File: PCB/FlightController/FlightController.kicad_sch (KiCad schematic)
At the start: 13 parts, among them J1 SMA Connector, J2 BATT IN, J3 BATT OUT, J4 BATT Reg IC, J5 Pump, J6 HallCircuit, U1 XIAO-nRF52840-DIP, U2 RFM95W

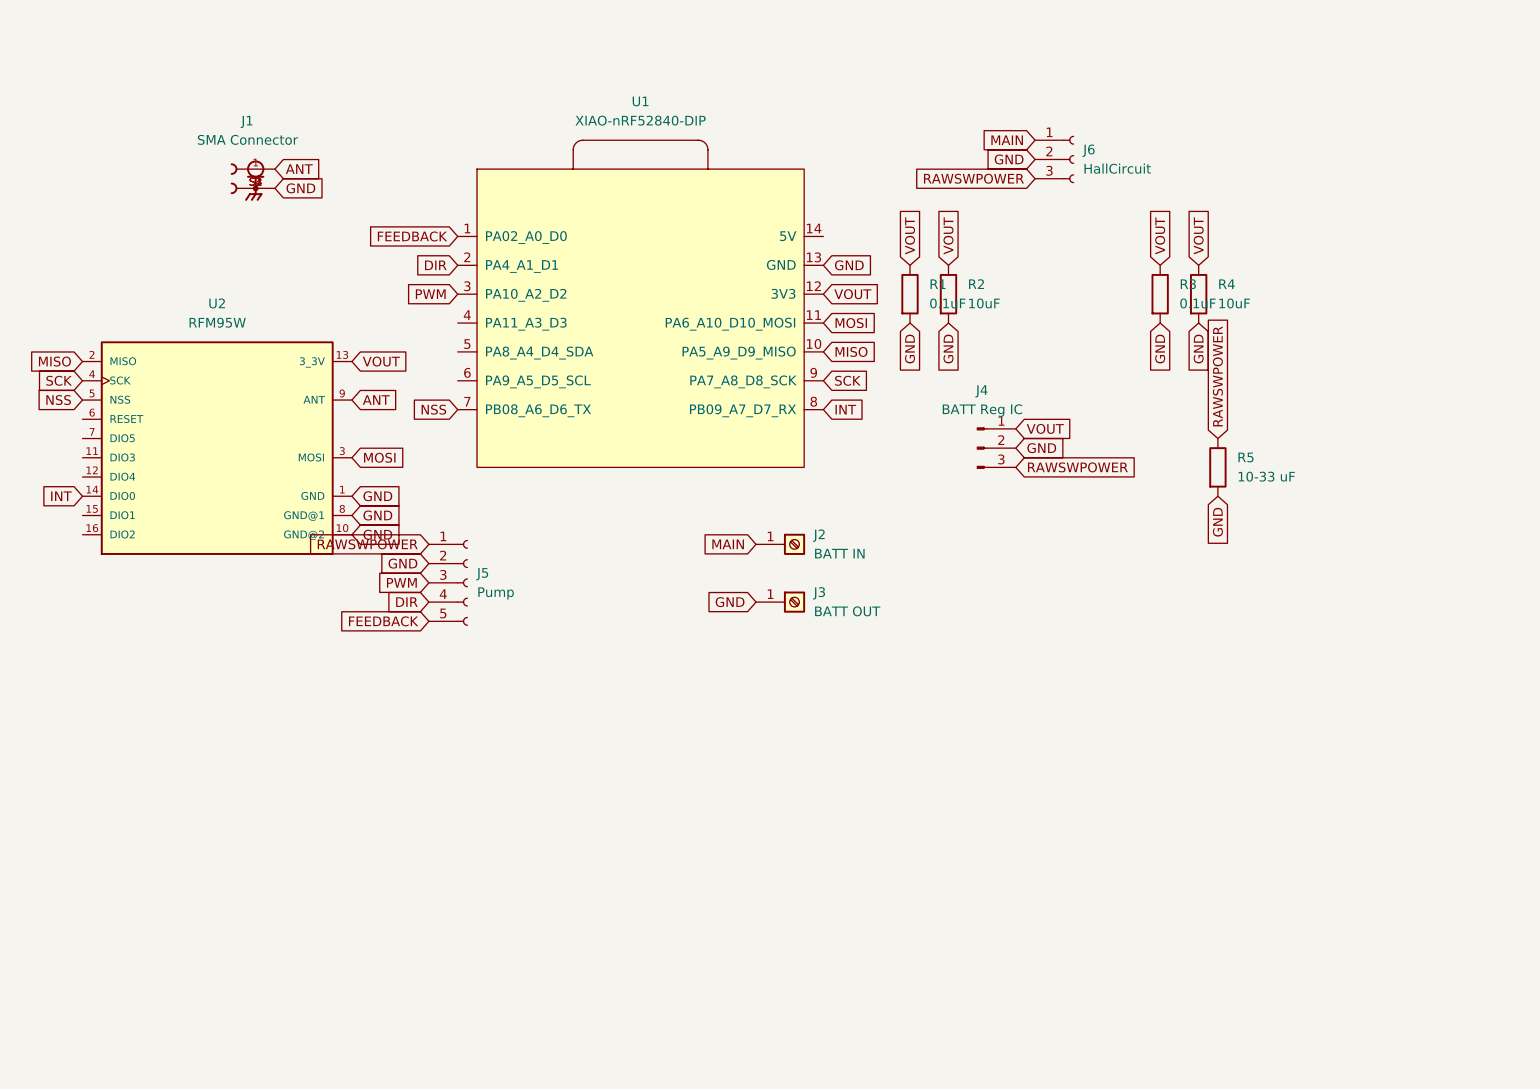
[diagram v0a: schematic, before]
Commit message: added a P-mosfet for the 3.3v wiring and let the 3.3v regulator "pre-power" the (now 4) pin switch system for the hall effect magnet sensor.
added a P-mosfet for the 3.3v wiring and let the 3.3v regulator "pre-power" the (now 4) pin switch system for the hall effect magnet sensor.
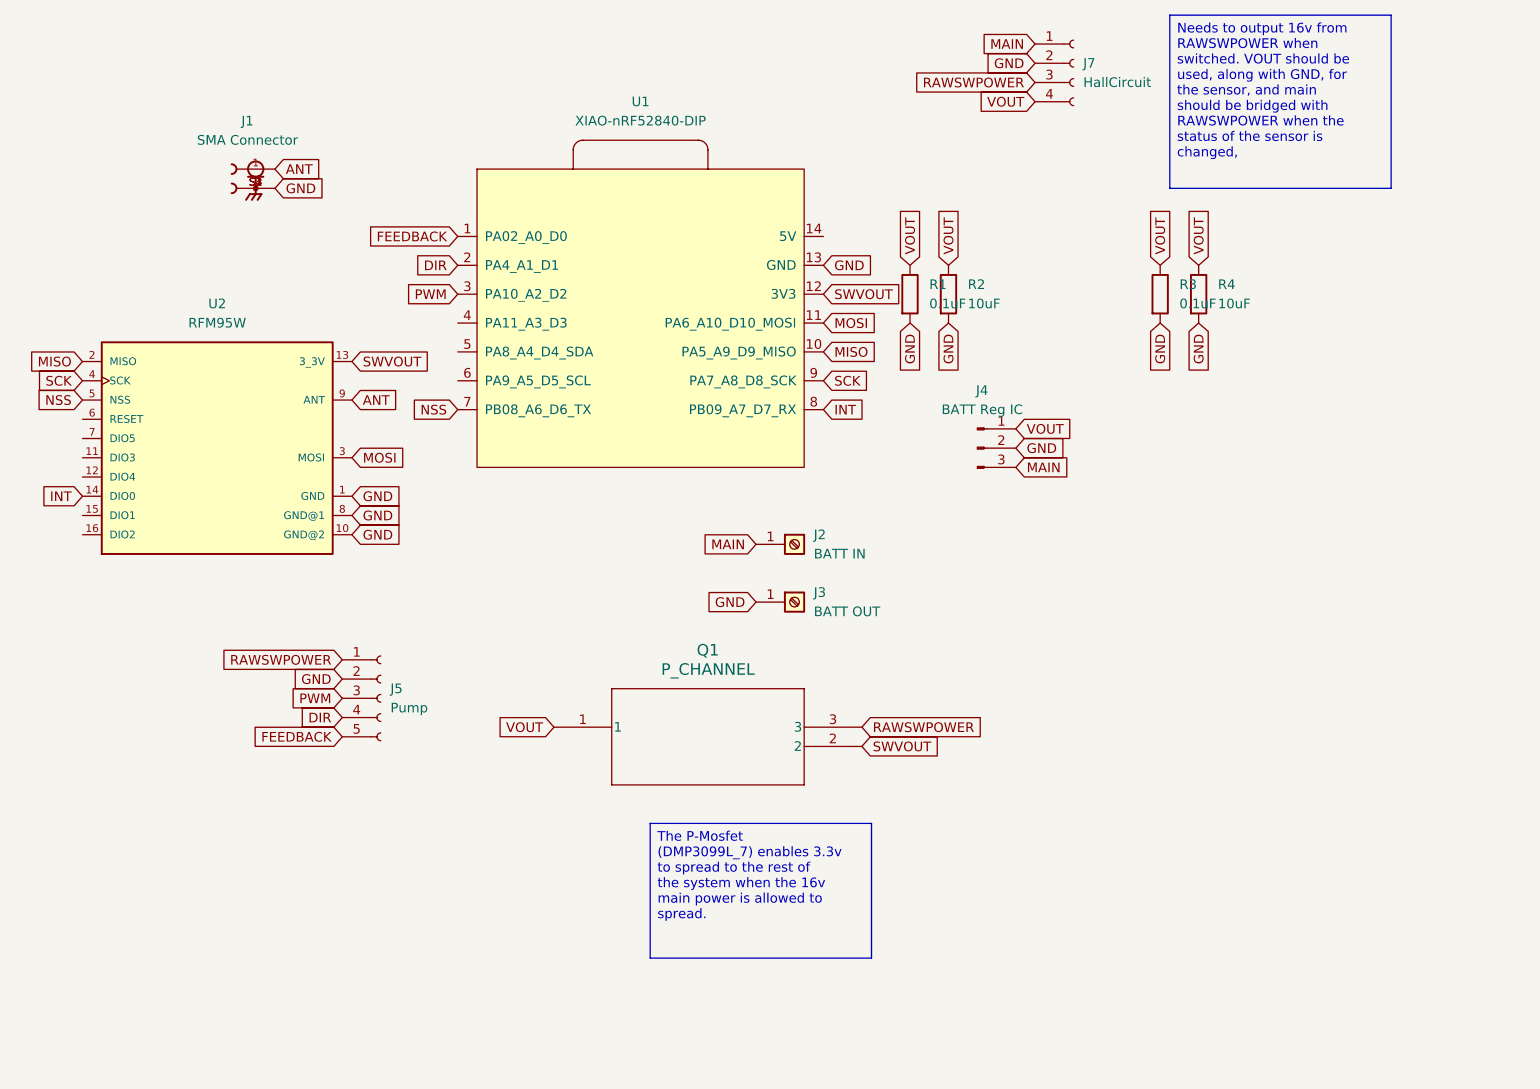
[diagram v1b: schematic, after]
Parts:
- removed J6: HallCircuit, Connector_PinHeader_2.54mm:PinHeader_1x03_P2.54mm_Vertical, symbol Connector:Conn_01x03_Socket
- removed R5: 10-33 uF, Resistor_SMD:R_0402_1005Metric_Pad0.72x0.64mm_HandSolder, symbol Device:R
- added J7: HallCircuit, Connector_PinHeader_2.54mm:PinHeader_1x04_P2.54mm_Vertical, symbol Connector:Conn_01x04_Socket
- added Q1: P_CHANNEL, DMP3099L_7:DMP3099L-7_DIO, symbol DMP3099L_7:DMP3099L-7
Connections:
- net GND: now also J7.2 (Pin_2)
- net MAIN: now also J4.3 (VIN), J7.1 (Pin_1)
- net RAWSWPOWER: now also J7.3 (Pin_3), Q1.3; no longer J4.3 (VIN)
- net VOUT: now also J7.4 (Pin_4), Q1.1; no longer U1.12 (3V3), U2.13 (3_3V)
- new net SWVOUT: Q1.2, U1.12 (3V3), U2.13 (3_3V)
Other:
- moved on the sheet: J5

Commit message: All boards should be finished. ACC otw, and an earlier version of the main board otw
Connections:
- net RAWSWPOWER: now also Q1.2; no longer Q1.3
- net SWVOUT: now also Q1.3; no longer Q1.2

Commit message: post R1 - flipped many traces and worked on adding an internal sensor for reduncancy
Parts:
- removed J5: Pump, Connector_PinHeader_2.54mm:PinHeader_1x05_P2.54mm_Vertical, symbol Connector:Conn_01x05_Socket
- removed R1: 0.1uF, Resistor_SMD:R_0402_1005Metric_Pad0.72x0.64mm_HandSolder, symbol Device:R
- removed R2: 10uF, Resistor_SMD:R_0402_1005Metric_Pad0.72x0.64mm_HandSolder, symbol Device:R
- added A1: MS583702BA01-50, MS583702BA01_50:XDCR_MS583702BA01-50, symbol MS583702BA01-50:MS583702BA01-50
- added J6: Pressure sensor, Connector_JST:JST_GH_BM04B-GHS-TBT_1x04-1MP_P1.25mm_Vertical, symbol Connector:Conn_01x04_Socket
- added J8: 530470510, 530470510:MOLEX_530470510, symbol 530470510:530470510
- added MOSFET1, MOSFET2: DMP3068L-7, DMP3068L_7:SOT-23_DMP3068L_DIO, symbol 2026-02-01_05-09-31:DMP3068L-7
- added R5, R6, R7: 4.7k, Resistor_SMD:R_0402_1005Metric_Pad0.72x0.64mm_HandSolder, symbol Device:R
- added R8: 10k, Resistor_SMD:R_0402_1005Metric_Pad0.72x0.64mm_HandSolder, symbol Device:R
- J1: footprint SMAFootprint:TE_5-1814832-2 -> SMAv2:CONN_RF2-04A-T-00-50-G_ADM
- U2: footprint RMF95W:XCVR_RFM95W-868S2 -> RF_Module:HOPERF_RFM9XW_THT
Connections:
- net DIR: now also J8.4
- net FEEDBACK: now also J8.5
- net GND: now also A1.1 (GND), J6.1 (Pin_1), J8.2
- net MAIN: now also MOSFET2.2 (S), R5.1
- net PWM: now also J8.3
- net RAWSWPOWER: now also J8.1, MOSFET2.3 (D); no longer Q1.2
- net VOUT: now also U1.12 (3V3), MOSFET1.2 (S), R8.1; no longer Q1.1, R3.1, R4.1
- net PWRSwitch: now reaches U1.4 (PA11_A3_D3)
- net PWRSwitch: now also MOSFET1.1 (G), MOSFET2.1 (G), R5.2, R6.1, R6.2, R7.1, R7.2, R8.2
- net SDA: now reaches U1.5 (PA8_A4_D4_SDA)
- net SDA: now also A1.4 (SDA), J6.2 (Pin_2), R5.1
- net SCL: now reaches U1.6 (PA9_A5_D5_SCL)
- net SCL: now also A1.3 (SCL), J6.3 (Pin_3), R6.1
- removed net SWVOUT: Q1.3, U1.12 (3V3), U2.13 (3_3V)
- new net SW3v3: A1.2 (VDD), J6.4 (Pin_4), MOSFET1.3 (D), R3.1, R4.1, R5.2, R6.2, U2.13 (3_3V)
